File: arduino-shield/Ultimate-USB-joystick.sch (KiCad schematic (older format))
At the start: 25 parts, among them P1 Power, P2 Analog, P3 Digital, P4 Digital

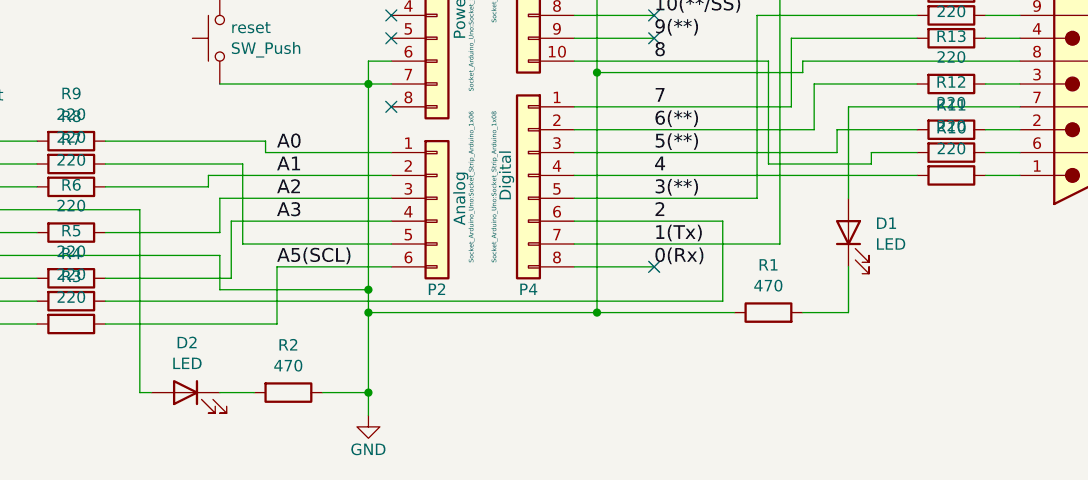
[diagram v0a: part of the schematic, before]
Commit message: increase R pad size, rename LED, fix reset switch
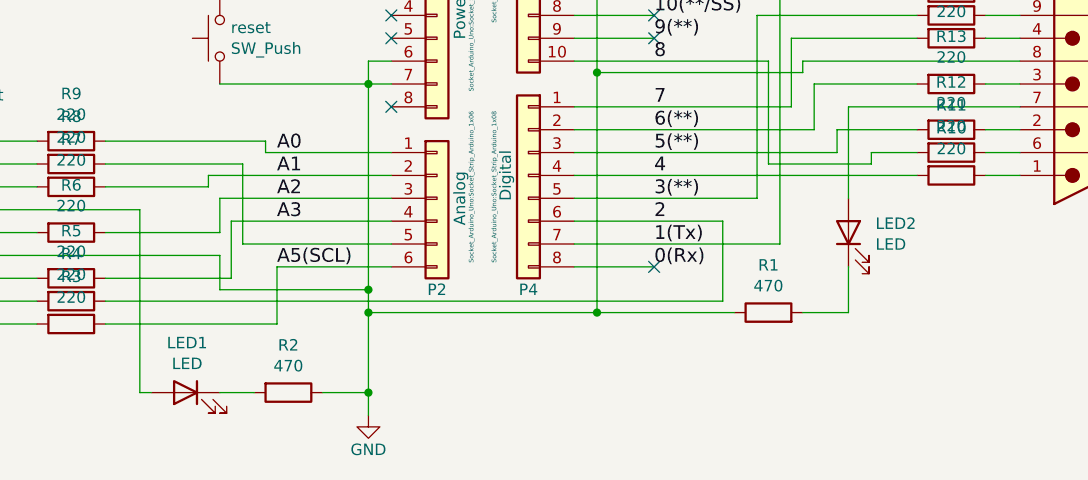
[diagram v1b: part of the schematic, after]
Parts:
- renumbered D2 to LED1, D1 to LED2
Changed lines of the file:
@@
 Connection ~ 5150 3250
 $Comp
-L Device:LED D1
+L Device:LED LED2
 U 1 1 5F5F196B
 P 6250 3950
-F 0 "D1" V 6289 3832 50  0000 R CNN
+F 0 "LED2" V 6289 3832 50  0000 R CNN
 F 1 "LED" V 6198 3832 50  0000 R CNN
 F 2 "LED_THT:LED_D5.0mm" H 6250 3950 50  0001 C CNN
@@
 	5050 3900 5700 3900
 $Comp
-L Device:LED D2
+L Device:LED LED1
 U 1 1 5F624294
 P 3350 4650
-F 0 "D2" H 3343 4867 50  0000 C CNN
+F 0 "LED1" H 3343 4867 50  0000 C CNN
 F 1 "LED" H 3343 4776 50  0000 C CNN
 F 2 "LED_THT:LED_D5.0mm" H 3350 4650 50  0001 C CNN
